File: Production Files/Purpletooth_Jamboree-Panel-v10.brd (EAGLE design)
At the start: 121.9 x 131.3 mm, 16 parts

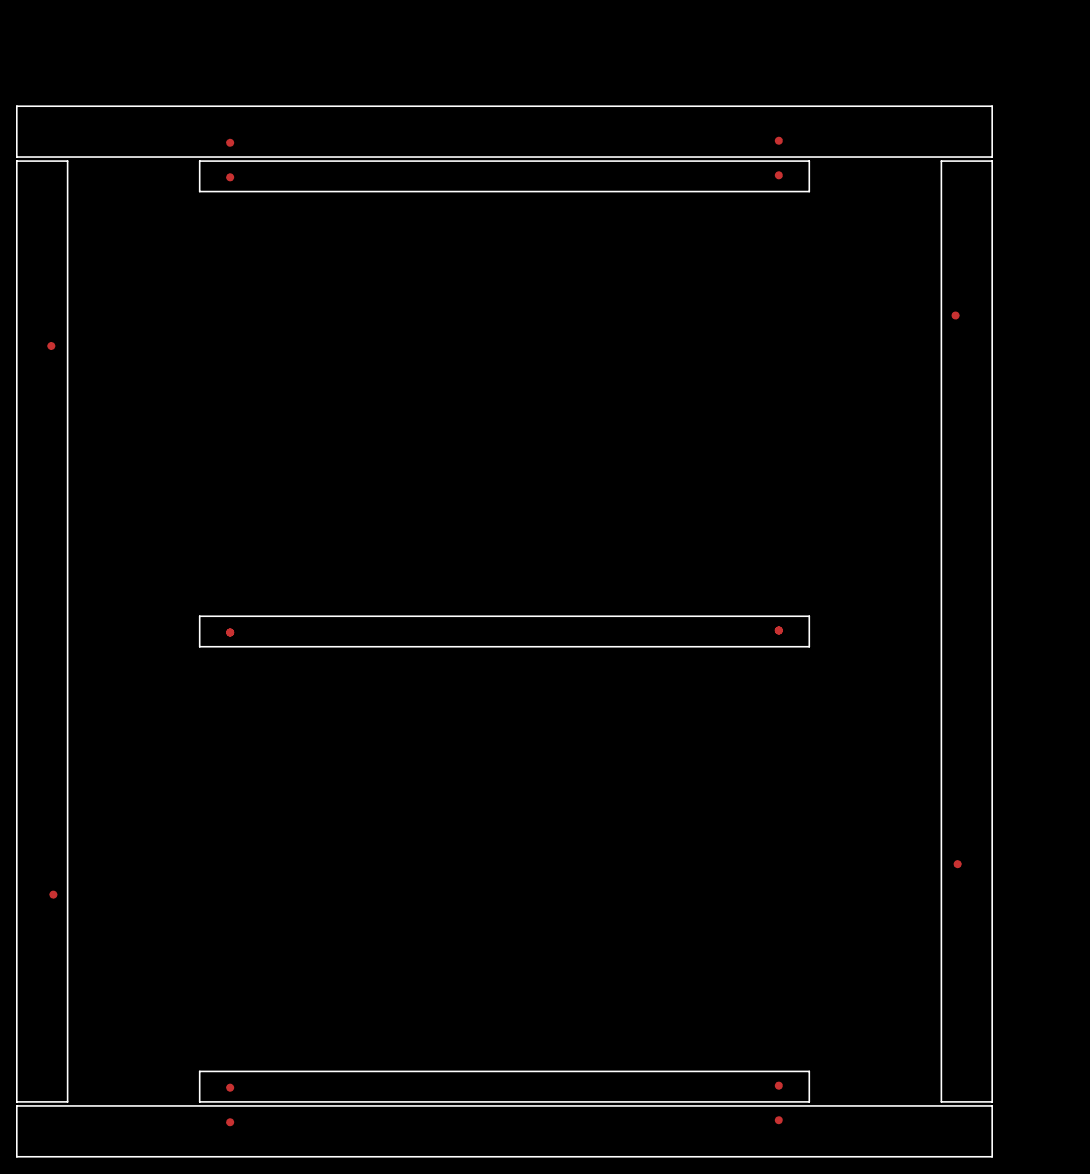
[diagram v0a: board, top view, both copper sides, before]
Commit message: Created Panel
normal sized panel
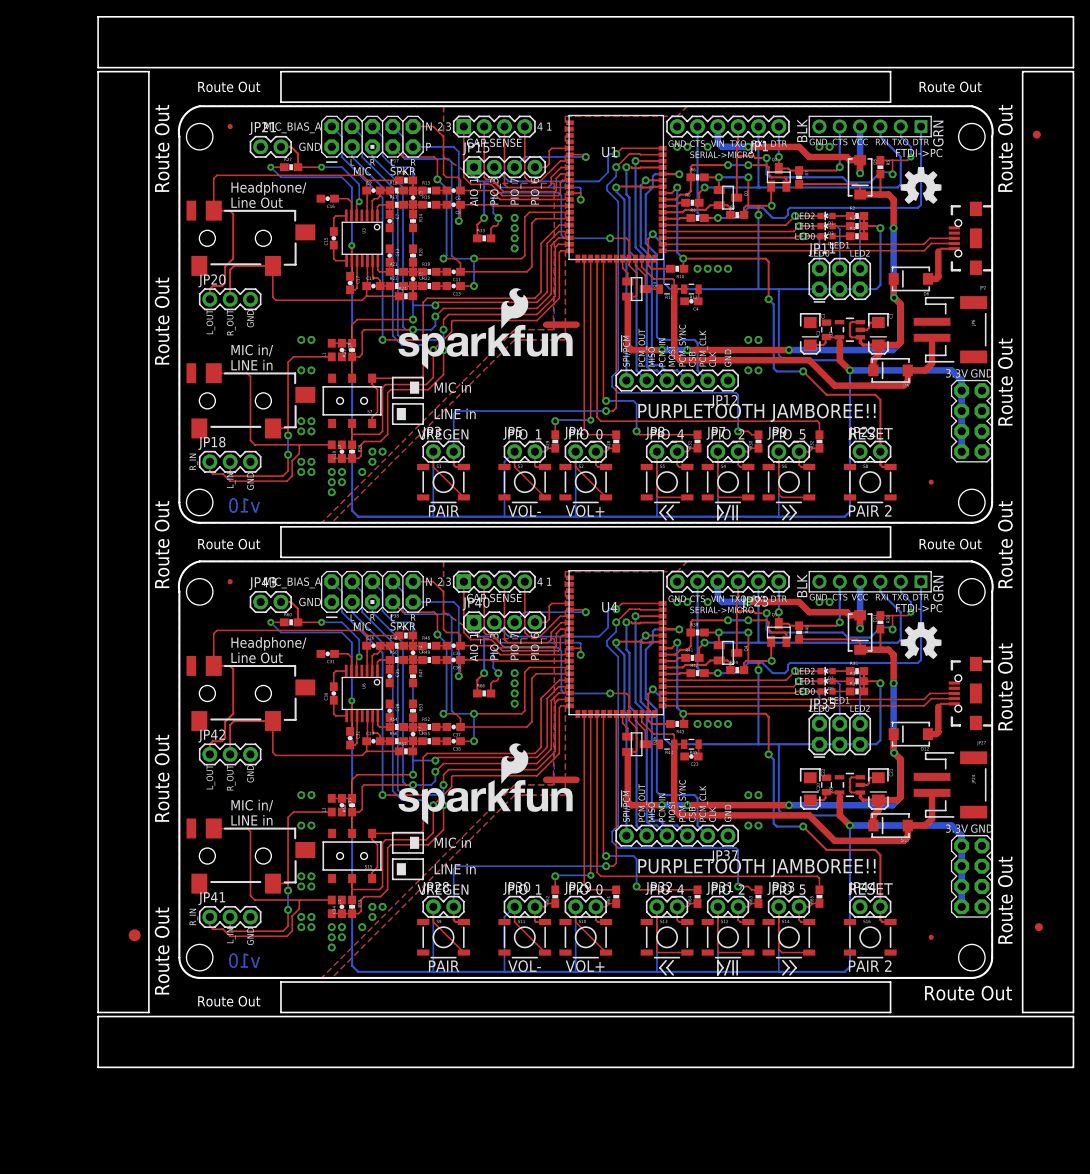
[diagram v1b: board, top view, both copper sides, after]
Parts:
- removed E$10, E$11, E$12, E$15, E$16, E$2, E$3, E$4, E$5, E$6, E$7, E$8, E$9: (no value), SparkFun-Aesthetics:FIDUCIAL-1X2
- added C1, C21, C22, C3: 10uF, SparkFun-Capacitors:EIA3216
- added C10, C24, C27, C5: 180pF, SparkFun-Capacitors:0603-CAP
- added C11, C13, C35, C36, C37, C38, C6, C8: 0.1uF, SparkFun-Capacitors:0603-CAP
- added C12, C14, C25, C26, C28, C29, C7, C9: 47pF, SparkFun-Capacitors:0603-CAP
- added C15, C16, C17, C30, C31, C32: 1.0uF, SparkFun-Capacitors:0603-CAP
- added C18, C19, C33, C34: 15pF, SparkFun-Capacitors:0603-CAP
- added C2, C20: 1uF, SparkFun-Capacitors:0805
- added C23, C4: 4.7uF, SparkFun-Capacitors:0603-CAP
- added D1, D7: GREEN, SparkFun-LED:LED-0603
- added D10, D11, D12, D4, D5, D6: BA340A, SparkFun-DiscreteSemi:SMA-DIODE
- added D2, D8: RED, SparkFun-LED:LED-0603
- added D3, D9: BLUE, SparkFun-LED:LED-0603
- added FID1, FID2, FID3, FID4: FIDUCIALUFIDUCIAL, SparkFun-Aesthetics:MICRO-FIDUCIAL
- added JP1, JP23: FTDI_BASICPTH, SparkFun-Connectors:FTDI_BASIC
- added JP10, JP15, JP34, JP40: (no value), SparkFun-Connectors:1X04
- added JP11, JP35: (no value), SparkFun-Connectors:2X3
- added JP12, JP37: (no value), SparkFun-Connectors:1X06
- added JP13, JP14, JP25, JP26: AUDIO-JACK2SMD, SparkFun-Connectors:AUDIO-JACK-3.5MM-SMD
- added JP16, JP36: M04X2, SparkFun-Connectors:2X4
- added JP17, JP38: M05X2PTH, SparkFun-Connectors:AVR_ICSP
- added JP18, JP20, JP41, JP42: (no value), SparkFun-Connectors:1X03
- added JP19, JP39: FTDI_DEVICE, SparkFun-Connectors:FTDI_DEVICE_SIDE
- added JP2, JP27: (no value), SparkFun-Connectors:USB-AB-MICRO-SMD_V03
- added JP21, JP22, JP28, JP29, JP3, JP30, JP31, JP32, JP33, JP4, JP43, JP44, JP5, JP7, JP8, JP9: M02PTH, SparkFun-Connectors:1X02
- added JP24, JP6: M02-JST-2MM-SMT, SparkFun-Connectors:JST-2-SMD
- added L1, L2, L3, L4: 15nH, SparkFun-Passives:0603
- added LOGO1, LOGO3: OSHW-LOGOM, SparkFun-Aesthetics:OSHW-LOGO-M
- added LOGO2, LOGO4: SFE_LOGO_NAME_FLAME.2_INCH, SparkFun-Aesthetics:SFE_LOGO_NAME_FLAME_.2
- added Q1, Q2, Q4, Q5: MOSFET-NCHANNELBSS138, SparkFun-DiscreteSemi:SOT23
- added Q3, Q6: MMBT4403, SparkFun-DiscreteSemi:SOT23
- added R1, R10, R27, R33, R34, R38, R39, R40, R41, R42, R43, R5, R6, R60, R66, R7, R8, R9: 10K, SparkFun-Resistors:0603-RES
- added R11, R44: 0.75, SparkFun-Resistors:0805
- added R12, R45: 0.22, SparkFun-Resistors:0805
- added R13, R16, R19, R22, R46, R49, R52, R55: 15K, SparkFun-Resistors:0603-RES
- added R14, R18, R20, R24, R47, R51, R53, R57: 30.1k, SparkFun-Resistors:0603-RES
- added R15, R17, R21, R23, R48, R50, R54, R56: 43k, SparkFun-Resistors:0603-RES
- added R2, R3, R35, R36, R37, R4: 240, SparkFun-Resistors:0603-RES
- added R25, R26, R28, R29, R30, R31, R32, R58, R59, R61, R62, R63, R64, R65: 2.2k, SparkFun-Resistors:0603-RES
- added S1, S10, S11, S12, S13, S14, S16, S2, S3, S4, S5, S6, S8, S9: (no value), SparkFun-Electromechanical:TACTILE_SWITCH_SMD
- added S15, S7: DPDT, SparkFun-Electromechanical:AYZ0202
- added STANDOFF1, STANDOFF2, STANDOFF3, STANDOFF4, STANDOFF5, STANDOFF6, STANDOFF7, STANDOFF8: STAND-OFF, SparkFun-Electromechanical:STAND-OFF
- added U1, U4: (no value), SparkFun-RF:BC127
- added U2, U5: MIC5219 3.3V, SparkFun-PowerIC:SOT23-5
- added U3, U6: TPA6138A2, SparkFun-AnalogIC:TSSOP-14
- E$1: device SparkFun-Aesthetics:FIDUCIAL-1X2 -> SparkFun-Aesthetics:FIDUCIAL-1.5X3
- moved E$1 89.1 mm to (4.57, 16.5), turned to 0 degrees
- moved E$13 24.8 mm to (117.3, 116.6)
- moved E$14 12.9 mm to (117.6, 17.5)
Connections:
- new net !RESET: JP22.2, R10.1, S8.2, U1.44
- new net !RESET1: JP44.2, R43.1, S16.2, U4.44
- new net 3.3V: C1.A, C17.1, C2.1, JP11.1, JP11.3, JP11.5, JP16.1, JP16.3, JP16.5, JP16.7, JP3.1, JP4.1, JP5.1, JP7.1, JP8.1, JP9.1, Q1.1, Q2.1, R1.2, R10.2, R2.2, R27.1, R3.2, R4.2, R6.2, S1.4, S2.4, S3.4, S4.4, S5.4, S6.4, U1.33, U2.5, U3.9
- new net 3.3V1: C20.1, C22.A, C32.1, JP28.1, JP29.1, JP30.1, JP31.1, JP32.1, JP33.1, JP35.1, JP35.3, JP35.5, JP36.1, JP36.3, JP36.5, JP36.7, Q4.1, Q5.1, R34.2, R35.2, R36.2, R37.2, R39.2, R43.2, R60.1, S10.4, S11.4, S12.4, S13.4, S14.4, S9.4, U4.33, U5.5, U6.9
- new net 5V_CTS: JP1.CTS, JP19.P$1, R9.2
- new net 5V_CTS1: JP23.CTS, JP39.P$1, R42.2
- new net 5V_RTS: JP1.DTR, JP19.P$5, Q2.3, R7.1
- new net 5V_RTS1: JP23.DTR, JP39.P$5, Q5.3, R40.1
- new net 5V_RX: JP1.RXI, JP19.P$3, R8.2
- new net 5V_RX1: JP23.RXI, JP39.P$3, R41.2
- new net 5V_TX: JP1.TXO, JP19.P$2, Q1.3, R5.1
- new net 5V_TX1: JP23.TXO, JP39.P$2, Q4.3, R38.1
- new net AIO_1: JP15.1, R33.1, U1.12
- new net AIO_2: JP40.1, R66.1, U4.12
- new net CAP_SENSE-1: JP34.3, U4.8
- new net CAP_SENSE-4: JP10.3, U1.8
- new net CAP_SENSE_1: JP10.4, U1.7
- new net CAP_SENSE_2: JP10.1, U1.10
- new net CAP_SENSE_3: JP10.2, U1.9
- new net CAP_SENSE_4: JP34.2, U4.9
- new net CAP_SENSE_5: JP34.4, U4.7
- new net CAP_SENSE_6: JP34.1, U4.10
- new net CHG_EXT: Q3.1, U1.29
- new net CHG_EXT1: Q6.1, U4.29
- new net CTS: R9.1, U1.40
- new net CTS1: R42.1, U4.40
- new net GND: C1.C, C12.1, C16.2, C17.2, C18.2, C19.2, C2.2, C3.C, C4.2, C7.2, JP1.GND, JP12.1, JP13.SLEEVE, JP14.SLEEVE, JP16.2, JP16.4, JP16.6, JP16.8, JP17.1, JP18.3, JP19.P$6, JP2.GND1, JP20.3, JP21.1, JP22.1, JP6.1, R14.2, R20.1, S7.3, S7.6, S8.4, U1.1, U1.11, U1.2, U1.22, U1.27, U1.3, U1.4, U2.2, U3.10, U3.4
- new net GND1: C20.2, C21.C, C22.C, C23.2, C25.2, C28.1, C31.2, C32.2, C33.2, C34.2, JP23.GND, JP24.1, JP25.SLEEVE, JP26.SLEEVE, JP27.GND1, JP36.2, JP36.4, JP36.6, JP36.8, JP37.1, JP38.1, JP39.P$6, JP41.3, JP42.3, JP43.1, JP44.1, R47.2, R53.1, S15.3, S15.6, S16.4, U4.1, U4.11, U4.2, U4.22, U4.27, U4.3, U4.4, U5.2, U6.10, U6.4
- new net LED_0: D2.C, JP11.2, U1.37
- new net LED_1: D3.C, JP11.4, U1.38
- new net LED_2: D1.C, JP11.6, U1.39
- new net LED_3: D7.C, JP35.6, U4.39
- new net LED_4: D9.C, JP35.4, U4.38
- new net LED_5: D8.C, JP35.2, U4.37
- new net L_IN: JP14.RING, JP18.1, L2.1
- new net L_IN1: JP26.RING, JP41.1, L4.1
- new net L_OUT: C9.1, JP13.RING, JP20.1, R18.1, U3.3
- new net L_OUT1: C26.1, JP25.RING, JP42.1, R51.1, U6.3
- new net MIC_BIAS_A: JP17.2, S7.1, S7.4, U1.17
- new net MIC_BIAS_A1: JP38.2, S15.1, S15.4, U4.17
- new net MIC_LN: C19.1, JP17.4, L2.2, R26.2, U1.20
- new net MIC_LN1: C34.1, JP38.4, L4.2, R59.2, U4.20
- new net MIC_LP: JP17.3, R26.1, S7.2, U1.21
- new net MIC_LP1: JP38.3, R59.1, S15.2, U4.21
- new net MIC_RN: C18.1, JP17.6, L1.2, R25.2, U1.18
- new net MIC_RN1: C33.1, JP38.6, L3.2, R58.2, U4.18
- new net MIC_RP: JP17.5, R25.1, S7.5, U1.19
- new net MIC_RP1: JP38.5, R58.1, S15.5, U4.19
- new net N$1: JP21.2, R27.2, U3.5
- new net N$10: JP4.2, R28.1, S2.2
- new net N$11: JP5.2, R29.1, S3.2
- new net N$12: C7.1, R17.1, U3.1
- new net N$13: C5.2, R14.1, R16.1, R17.2
- new net N$14: JP7.2, R30.1, S4.2
- new net N$15: JP8.2, R31.1, S5.2
- new net N$16: C10.1, R19.1, R20.2, R21.2
- new net N$17: C12.2, R21.1, U3.14
- new net N$18: C11.2, R19.2
- new net N$19: C10.2, R22.1, R23.2, R24.2
- new net N$2: D3.A, R3.1
- new net N$20: C13.2, R22.2
- new net N$21: C14.2, R23.1, U3.13
- new net N$22: JP9.2, R32.1, S6.2
- new net N$23: D8.A, R37.1
- new net N$24: C16.1, U3.6
- new net N$25: C15.2, U3.7
- new net N$26: C15.1, U3.8
- new net N$27: D7.A, R35.1
- new net N$28: C4.1, R12.1
- new net N$29: C23.1, R45.1
- new net N$3: D9.A, R36.1
- new net N$30: C36.2, R49.2
- new net N$31: C35.2, R46.2
- new net N$32: C24.1, R46.1, R48.2, R51.2
- new net N$33: C26.2, R48.1, U6.2
- new net N$34: C25.1, R50.1, U6.1
- new net N$35: C24.2, R47.1, R49.1, R50.2
- new net N$36: C27.1, R52.1, R53.2, R54.2
- new net N$37: C28.2, R54.1, U6.14
- new net N$38: C37.2, R52.2
- new net N$39: C27.2, R55.1, R56.2, R57.2
- new net N$4: C8.2, R16.2
- new net N$40: C38.2, R55.2
- new net N$41: C29.2, R56.1, U6.13
- new net N$42: C31.1, U6.6
- new net N$43: C30.2, U6.7
- new net N$44: C30.1, U6.8
- new net N$45: JP43.2, R60.2, U6.5
- new net N$46: JP29.2, R61.1, S10.2
- new net N$47: JP30.2, R62.1, S11.2
- new net N$48: JP31.2, R63.1, S12.2
- new net N$49: JP32.2, R64.1, S13.2
- new net N$5: C6.2, R13.2
- new net N$50: JP33.2, R65.1, S14.2
- new net N$6: D2.A, R4.1
- new net N$7: D1.A, R2.1
- new net N$8: C5.1, R13.1, R15.2, R18.2
- new net N$9: C9.2, R15.1, U3.2
- new net PCM_CLK/CLK: JP12.2, U1.47
- new net PCM_CLK/CLK1: JP37.2, U4.47
- new net PCM_IN/MOSI: JP12.4, U1.49
- new net PCM_IN/MOSI1: JP37.4, U4.49
- new net PCM_OUT/MISO: JP12.5, U1.48
- new net PCM_OUT/MISO1: JP37.5, U4.48
- new net PCM_SYNC/CSB: JP12.3, U1.46
- new net PCM_SYNC/CSB1: JP37.3, U4.46
- new net PIO_0: R28.2, U1.23
- new net PIO_1: R29.2, U1.24
- new net PIO_10: JP40.4, U4.5
- new net PIO_11: JP40.3, U4.6
- new net PIO_12: R64.2, U4.26
- new net PIO_13: JP40.2, U4.51
- new net PIO_14: R63.2, U4.50
- new net PIO_15: R62.2, U4.24
- new net PIO_2: R30.2, U1.50
- new net PIO_3: JP15.2, U1.51
- new net PIO_4: R31.2, U1.26
- new net PIO_5: R32.2, U1.25
- new net PIO_6: JP15.4, U1.5
- new net PIO_7: JP15.3, U1.6
- new net PIO_8: R61.2, U4.23
- new net PIO_9: R65.2, U4.25
- new net RTS: Q2.2, R6.1, U1.43
- new net RTS1: Q5.2, R39.1, U4.43
- new net RX: R8.1, U1.42
- new net RX1: R41.1, U4.42
- new net R_IN: JP14.TIP, JP18.2, L1.1
- new net R_IN1: JP26.TIP, JP41.2, L3.1
- new net R_OUT: C14.1, JP13.TIP, JP20.2, R24.1, U3.12
- new net R_OUT1: C29.1, JP25.TIP, JP42.2, R57.1, U6.12
- new net SPI_!PCM: JP12.6, U1.45
- new net SPI_!PCM1: JP37.6, U4.45
- new net SPKR_LN: C6.1, JP17.10, U1.13
- new net SPKR_LN1: C35.1, JP38.10, U4.13
- new net SPKR_LP: C8.1, JP17.9, U1.14
- new net SPKR_LP1: C36.1, JP38.9, U4.14
- new net SPKR_RN: C13.1, JP17.8, U1.15
- new net SPKR_RN1: C38.1, JP38.8, U4.15
- new net SPKR_RP: C11.1, JP17.7, U1.16
- new net SPKR_RP1: C37.1, JP38.7, U4.16
- new net TX: Q1.2, R1.1, U1.41
- new net TX1: Q4.2, R34.1, U4.41
- new net USB_N: JP2.D-1, U1.35
- new net USB_N1: JP27.D-1, U4.35
- new net USB_P: JP2.D+1, U1.36
- new net USB_P1: JP27.D+1, U4.36
- new net VBAT_SENSE: Q3.3, R11.2, U1.31
- new net VBAT_SENSE1: Q6.3, R44.2, U4.31
- new net VIN: C3.A, D4.C, D5.C, D6.C, Q3.2, R33.2, R5.2, R7.2, U1.30, U2.1, U2.3
- new net VIN1: C21.A, D10.C, D11.C, D12.C, Q6.2, R38.2, R40.2, R66.2, U4.30, U5.1, U5.3
- new net VREGEN: JP3.2, S1.2, U1.28
- new net VREGEN1: JP28.2, S9.2, U4.28
- new net V_BAT: D4.A, JP6.2, R11.1, R12.2, U1.32
- new net V_BAT1: D10.A, JP24.2, R44.1, R45.2, U4.32
- new net V_FTDI: D5.A, JP1.VCC, JP19.P$4
- new net V_FTDI1: D11.A, JP23.VCC, JP39.P$4
- new net V_USB: D6.A, JP2.VBUS1
- new net V_USB1: D12.A, JP27.VBUS1
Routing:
- net 3.3V: track 0.00 -> 372.9 mm, vias 0 -> 9
- net 3.3V1: track 0.00 -> 372.9 mm, vias 0 -> 9
- net VIN1: track 0.00 -> 133.6 mm, vias 0 -> 7
- net VIN: track 0.00 -> 133.6 mm, vias 0 -> 7
- net MIC_LN1: track 0.00 -> 86.8 mm, vias 0 -> 2
- net MIC_LN: track 0.00 -> 86.8 mm, vias 0 -> 2
- net MIC_BIAS_A: track 0.00 -> 82.2 mm, vias 0 -> 1
- net MIC_BIAS_A1: track 0.00 -> 82.2 mm, vias 0 -> 1
- net MIC_LP1: track 0.00 -> 80.2 mm, vias 0 -> 1
- net MIC_LP: track 0.00 -> 80.2 mm, vias 0 -> 1
- net MIC_RP1: track 0.00 -> 67.4 mm, vias 0 -> 2
- net MIC_RP: track 0.00 -> 67.4 mm, vias 0 -> 2
- net MIC_RN1: track 0.00 -> 67.2 mm, vias 0 -> 2
- net MIC_RN: track 0.00 -> 67.2 mm, vias 0 -> 2
- net !RESET1: track 0.00 -> 61.5 mm, vias 0 -> 4
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- added copper zone on layer 1, net GND
- added copper zone on layer 16, net GND
- added copper zone on layer 1, net GND1
- added copper zone on layer 16, net GND1
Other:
- outline, holes or cut-outs redrawn
- board text added: "1"
- board text added: "2"
- board text added: "3"
- board text added: "3.3V"
- board text added: "4"
- board text added: "AIO_1"
- board text added: "CAP SENSE"
- board text added: "CTS"
- board text added: "DTR"
- board text added: "FTDI->PC"
- board text added: "GND"
- board text added: "Headphone/ Line Out"
- board text added: "L"
- board text added: "LED0"
- board text added: "LED1"
- board text added: "LED2"
- board text added: "LINE in"
- board text added: "L_IN"
- board text added: "L_OUT"
- board text added: "MIC"
- board text added: "MIC in"
- board text added: "MIC in/ LINE in"
- board text added: "MIC_BIAS_A"
- board text added: "N"
- board text added: "P"
- board text added: "PAIR"
- board text added: "PAIR 2"
- board text added: "PCM_CLK CLK"
- board text added: "PCM_IN MOSI"
- board text added: "PCM_OUT MISO"
- board text added: "PCM_SYNC CSB"
- board text added: "PIO_0"
- board text added: "PIO_1"
- board text added: "PIO_2"
- board text added: "PIO_3"
- board text added: "PIO_4"
- board text added: "PIO_5"
- board text added: "PIO_6"
- board text added: "PIO_7"
- board text added: "PURPLETOOTH JAMBOREE!!"
- board text added: "R"
- board text added: "RESET"
- board text added: "RXI"
- board text added: "R_IN"
- board text added: "R_OUT"
- board text added: "Route Out"
- board text added: "SERIAL->MICRO"
- board text added: "SPI/!PCM"
- board text added: "SPKR"
- board text added: "TXO"
- board text added: "VIN"
- board text added: "VOL+"
- board text added: "VOL-"
- board text added: "VREGEN"
- board text added: "v10"

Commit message: added over paste for the module to panel
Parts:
- U1, U4: device SparkFun-RF:BC127 -> SparkFun-RF:BC127_XTRA_PASTE
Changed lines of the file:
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@@
 <element name="E$13" library="SparkFun-Aesthetics" package="FIDUCIAL-1X2" value="" x="117.348" y="116.586" smashed="yes" rot="R180"/>
 <element name="E$14" library="SparkFun-Aesthetics" package="FIDUCIAL-1X2" value="" x="117.602" y="17.526" smashed="yes"/>
-<element name="U1" library="SparkFun-RF" package="BC127" value="" x="64.77" y="109.982" smashed="yes">
+<element name="U1" library="SparkFun-RF" package="BC127_XTRA_PASTE" value="" x="64.77" y="109.982" smashed="yes">
 <attribute name="NAME" x="62.87" y="113.782" size="1.27" layer="25"/>
 <attribute name="VALUE" x="62.87" y="112.182" size="1.27" layer="27"/>
@@
 <element name="FID1" library="SparkFun-Aesthetics" package="MICRO-FIDUCIAL" value="FIDUCIALUFIDUCIAL" x="16.51" y="117.602" smashed="yes"/>
 <element name="FID2" library="SparkFun-Aesthetics" package="MICRO-FIDUCIAL" value="FIDUCIALUFIDUCIAL" x="104.14" y="73.152" smashed="yes"/>
-<element name="U4" library="SparkFun-RF" package="BC127" value="" x="64.77" y="53.086" smashed="yes">
+<element name="U4" library="SparkFun-RF" package="BC127_XTRA_PASTE" value="" x="64.77" y="53.086" smashed="yes">
 <attribute name="NAME" x="62.87" y="56.886" size="1.27" layer="25"/>
 <attribute name="VALUE" x="62.87" y="55.286" size="1.27" layer="27"/>
